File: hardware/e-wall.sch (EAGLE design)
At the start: 23 parts, among them IC1 74HCT595N, IC2 74HCT595N, IC3 74HCT595N, IC4 ULN2803, IC5 ULN2803, IC6 ULN2803, T1 BC547, T2 BC557, T3 BC547

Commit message: Package der Widerstände geändert
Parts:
- R1, R2, R3, R6, R7, R8, R9: device resistor:R-EU_0309/10 -> resistor:R-EU_0207/7
- R4: device resistor:R-EU_0309/10 -> resistor:R-EU_0207/2V
- R5: device resistor:R-EU_0309/V -> resistor:R-EU_0207/2V
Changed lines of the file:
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@@
 <part name="GND8" library="supply1" deviceset="GND" device=""/>
 <part name="P+8" library="supply1" deviceset="+12V" device=""/>
-<part name="R1" library="resistor" deviceset="R-EU_" device="0309/10" value="20k"/>
-<part name="R2" library="resistor" deviceset="R-EU_" device="0309/10" value="30k"/>
-<part name="R3" library="resistor" deviceset="R-EU_" device="0309/10" value="110k"/>
-<part name="R4" library="resistor" deviceset="R-EU_" device="0309/10" value="NB"/>
+<part name="R1" library="resistor" deviceset="R-EU_" device="0207/7" value="20k"/>
+<part name="R2" library="resistor" deviceset="R-EU_" device="0207/7" value="30k"/>
+<part name="R3" library="resistor" deviceset="R-EU_" device="0207/7" value="110k"/>
+<part name="R4" library="resistor" deviceset="R-EU_" device="0207/2V" value="NB"/>
 <part name="T1" library="transistor" deviceset="*-NPN-" device="TO92-EBC" value="BC547"/>
 <part name="GND28" library="supply1" deviceset="GND" device=""/>
@@
 <part name="P+28" library="supply1" deviceset="VCC" device=""/>
 <part name="T2" library="transistor" deviceset="*-PNP-" device="TO92-BEC" value="BC557"/>
-<part name="R6" library="resistor" deviceset="R-EU_" device="0309/10" value="4.7k"/>
+<part name="R6" library="resistor" deviceset="R-EU_" device="0207/7" value="4.7k"/>
 <part name="GND30" library="supply1" deviceset="GND" device=""/>
 <part name="P+29" library="supply1" deviceset="VCC" device=""/>
-<part name="R5" library="resistor" deviceset="R-EU_" device="0309/V" value="6.2k"/>
+<part name="R5" library="resistor" deviceset="R-EU_" device="0207/2V" value="6.2k"/>
 <part name="T3" library="transistor" deviceset="*-NPN-" device="TO92-EBC" value="BC547"/>
-<part name="R7" library="resistor" deviceset="R-EU_" device="0309/10" value="7.5k"/>
+<part name="R7" library="resistor" deviceset="R-EU_" device="0207/7" value="7.5k"/>
 <part name="GND31" library="supply1" deviceset="GND" device=""/>
 <part name="SV1" library="con-lsta" deviceset="FE08-2" device=""/>
@@
 <part name="IC5" library="uln-udn" deviceset="ULN2803A" device="" value="ULN2803"/>
 <part name="IC6" library="uln-udn" deviceset="ULN2803A" device="" value="ULN2803"/>
-<part name="GND6" library="supply1" deviceset="GND" device=""/>
 <part name="GND7" library="supply1" deviceset="GND" device=""/>
 <part name="P+4" library="supply1" deviceset="VCC" device=""/>
-<part name="P+5" library="supply1" deviceset="VCC" device=""/>
-<part name="R8" library="resistor" deviceset="R-EU_" device="0309/10" value="20k"/>
-<part name="R9" library="resistor" deviceset="R-EU_" device="0309/10" value="30k"/>
+<part name="R8" library="resistor" deviceset="R-EU_" device="0207/7" value="20k"/>
+<part name="R9" library="resistor" deviceset="R-EU_" device="0207/7" value="30k"/>
 <part name="GND9" library="supply1" deviceset="GND" device=""/>
 <part name="U$2" library="ultrasonic" deviceset="HC-SR04" device=""/>
@@
 <instance part="IC5" gate="G$1" x="185.42" y="66.04" rot="MR180"/>
 <instance part="IC6" gate="G$1" x="185.42" y="27.94" rot="MR180"/>
-<instance part="GND6" gate="1" x="96.52" y="35.56"/>
 <instance part="GND7" gate="1" x="96.52" y="68.58"/>
 <instance part="P+4" gate="VCC" x="66.04" y="78.74"/>
-<instance part="P+5" gate="VCC" x="99.06" y="50.8"/>
 <instance part="R8" gate="G$1" x="104.14" y="30.48" rot="R90"/>
 <instance part="R9" gate="G$1" x="104.14" y="15.24" rot="R90"/>
@@
 <wire x1="96.52" y1="73.66" x2="96.52" y2="71.12" width="0.1524" layer="91"/>
 <pinref part="U$1" gate="G$1" pin="20"/>
-</segment>
-<segment>
-<pinref part="GND6" gate="1" pin="GND"/>
-<wire x1="88.9" y1="45.72" x2="96.52" y2="45.72" width="0.1524" layer="91"/>
-<wire x1="96.52" y1="45.72" x2="96.52" y2="43.18" width="0.1524" layer="91"/>
-<wire x1="96.52" y1="43.18" x2="96.52" y2="38.1" width="0.1524" layer="91"/>
-<wire x1="88.9" y1="43.18" x2="96.52" y2="43.18" width="0.1524" layer="91"/>
-<junction x="96.52" y="43.18"/>
 </segment>
 <segment>
@@
 </segment>
 <segment>
-<pinref part="P+5" gate="VCC" pin="VCC"/>
-<wire x1="88.9" y1="40.64" x2="99.06" y2="40.64" width="0.1524" layer="91"/>
-<wire x1="99.06" y1="40.64" x2="99.06" y2="48.26" width="0.1524" layer="91"/>
-</segment>
-<segment>

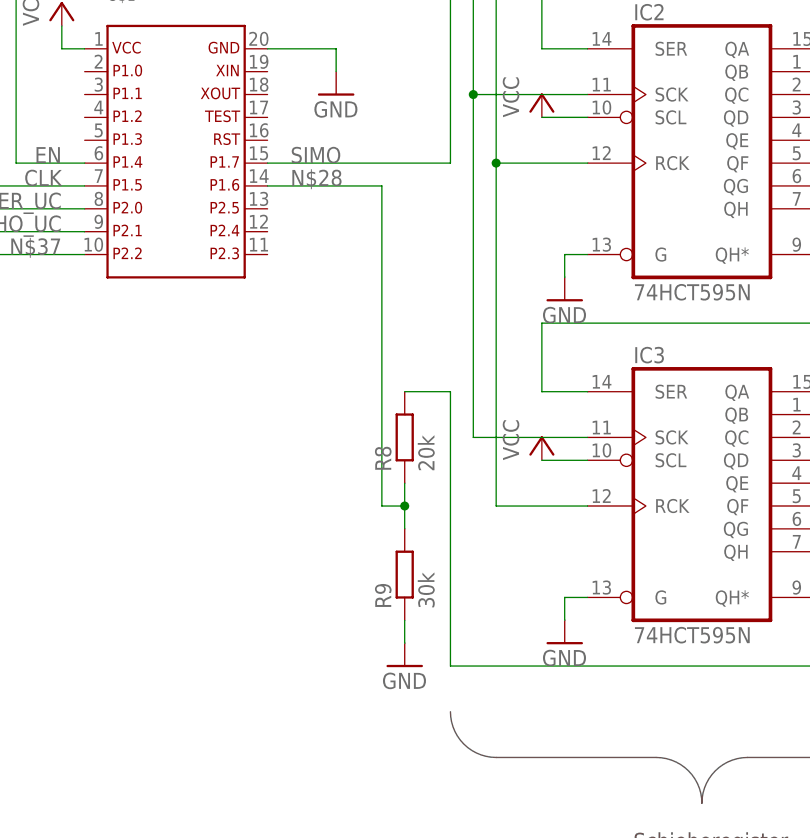
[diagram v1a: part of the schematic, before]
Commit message: Leitungen für SPI umbenannt
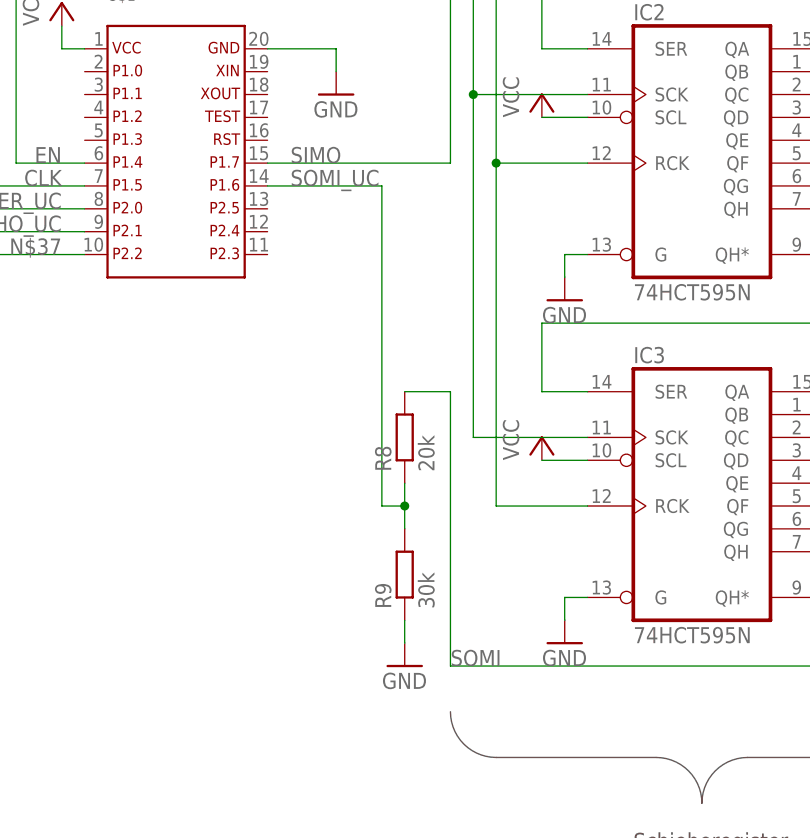
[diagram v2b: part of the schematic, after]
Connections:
- net N$28 renamed SOMI_UC
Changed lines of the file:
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@@
 <grid distance="0.1" unitdist="inch" unit="inch" style="lines" multiple="1" display="no" altdistance="0.01" altunitdist="inch" altunit="inch"/>
 <layers>
-<layer number="1" name="Top" color="4" fill="1" visible="yes" active="no"/>
-<layer number="16" name="Bottom" color="1" fill="1" visible="yes" active="no"/>
-<layer number="17" name="Pads" color="2" fill="1" visible="yes" active="no"/>
-<layer number="18" name="Vias" color="2" fill="1" visible="yes" active="no"/>
-<layer number="19" name="Unrouted" color="6" fill="1" visible="yes" active="no"/>
-<layer number="20" name="Dimension" color="15" fill="1" visible="yes" active="no"/>
-<layer number="21" name="tPlace" color="7" fill="1" visible="yes" active="no"/>
-<layer number="22" name="bPlace" color="7" fill="1" visible="yes" active="no"/>
-<layer number="23" name="tOrigins" color="15" fill="1" visible="yes" active="no"/>
-<layer number="24" name="bOrigins" color="15" fill="1" visible="yes" active="no"/>
-<layer number="25" name="tNames" color="7" fill="1" visible="yes" active="no"/>
-<layer number="26" name="bNames" color="7" fill="1" visible="yes" active="no"/>
-<layer number="27" name="tValues" color="7" fill="1" visible="yes" active="no"/>
-<layer number="28" name="bValues" color="7" fill="1" visible="yes" active="no"/>
+<layer number="1" name="Top" color="4" fill="1" visible="no" active="no"/>
+<layer number="16" name="Bottom" color="1" fill="1" visible="no" active="no"/>
+<layer number="17" name="Pads" color="2" fill="1" visible="no" active="no"/>
+<layer number="18" name="Vias" color="2" fill="1" visible="no" active="no"/>
+<layer number="19" name="Unrouted" color="6" fill="1" visible="no" active="no"/>
+<layer number="20" name="Dimension" color="15" fill="1" visible="no" active="no"/>
+<layer number="21" name="tPlace" color="7" fill="1" visible="no" active="no"/>
+<layer number="22" name="bPlace" color="7" fill="1" visible="no" active="no"/>
+<layer number="23" name="tOrigins" color="15" fill="1" visible="no" active="no"/>
+<layer number="24" name="bOrigins" color="15" fill="1" visible="no" active="no"/>
+<layer number="25" name="tNames" color="7" fill="1" visible="no" active="no"/>
+<layer number="26" name="bNames" color="7" fill="1" visible="no" active="no"/>
+<layer number="27" name="tValues" color="7" fill="1" visible="no" active="no"/>
+<layer number="28" name="bValues" color="7" fill="1" visible="no" active="no"/>
 <layer number="29" name="tStop" color="7" fill="3" visible="no" active="no"/>
 <layer number="30" name="bStop" color="7" fill="6" visible="no" active="no"/>
@@
 <layer number="35" name="tGlue" color="7" fill="4" visible="no" active="no"/>
 <layer number="36" name="bGlue" color="7" fill="5" visible="no" active="no"/>
-<layer number="37" name="tTest" color="7" fill="1" visible="yes" active="no"/>
-<layer number="38" name="bTest" color="7" fill="1" visible="yes" active="no"/>
+<layer number="37" name="tTest" color="7" fill="1" visible="no" active="no"/>
+<layer number="38" name="bTest" color="7" fill="1" visible="no" active="no"/>
 <layer number="39" name="tKeepout" color="4" fill="11" visible="no" active="no"/>
 <layer number="40" name="bKeepout" color="1" fill="11" visible="no" active="no"/>
@@
 <layer number="44" name="Drills" color="7" fill="1" visible="no" active="no"/>
 <layer number="45" name="Holes" color="7" fill="1" visible="no" active="no"/>
-<layer number="46" name="Milling" color="3" fill="1" visible="yes" active="no"/>
-<layer number="47" name="Measures" color="7" fill="1" visible="yes" active="no"/>
-<layer number="48" name="Document" color="7" fill="1" visible="yes" active="no"/>
-<layer number="49" name="Reference" color="7" fill="1" visible="yes" active="no"/>
-<layer number="51" name="tDocu" color="7" fill="1" visible="yes" active="no"/>
-<layer number="52" name="bDocu" color="7" fill="1" visible="yes" active="no"/>
+<layer number="46" name="Milling" color="3" fill="1" visible="no" active="no"/>
+<layer number="47" name="Measures" color="7" fill="1" visible="no" active="no"/>
+<layer number="48" name="Document" color="7" fill="1" visible="no" active="no"/>
+<layer number="49" name="Reference" color="7" fill="1" visible="no" active="no"/>
+<layer number="51" name="tDocu" color="7" fill="1" visible="no" active="no"/>
+<layer number="52" name="bDocu" color="7" fill="1" visible="no" active="no"/>
 <layer number="91" name="Nets" color="2" fill="1" visible="yes" active="yes"/>
 <layer number="92" name="Busses" color="1" fill="1" visible="yes" active="yes"/>
@@
 <pinref part="R8" gate="G$1" pin="2"/>
 <wire x1="104.14" y1="35.56" x2="109.22" y2="35.56" width="0.1524" layer="91"/>
+<label x="109.22" y="5.08" size="1.778" layer="95"/>
 </segment>
 </net>
@@
 </segment>
 </net>
-<net name="N$28" class="0">
+<net name="SOMI_UC" class="0">
 <segment>
 <wire x1="101.6" y1="58.42" x2="88.9" y2="58.42" width="0.1524" layer="91"/>
